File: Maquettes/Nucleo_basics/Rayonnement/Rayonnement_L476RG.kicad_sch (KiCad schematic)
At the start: 26 parts, among them J10 Morpho_Gauche, J11 Morpho_Droite, J19 GND_reg, J2 LED_POWER, J20 3.3V_reg, J23 D_IN_OUT, J7 Servo, J8 BAT_IN, Q1 IRLZ44N, SW1 SW_1, SW2 SW_2, U1 CNY17-3, U2 LM7805_TO220

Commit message: Update Rayonnement Schematics
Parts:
- removed Q1: IRLZ44N, Package_TO_SOT_THT:TO-220-3_Vertical, symbol Transistor_FET:IRLZ44N
- removed R4: 1k, symbol Device:R
- removed R6: 220, symbol Device:R
- removed U1: CNY17-3, symbol Isolator:CNY17-3
- added J1: LED_IN, TerminalBlock_Phoenix:TerminalBlock_Phoenix_MKDS-3-2-5.08_1x02_P5.08mm_Horizontal, symbol Connector_Generic:Conn_01x02
- added U1, U4: ~, Package_DIP:DIP-8_W7.62mm_LongPads, symbol LEnsE_devices:MCP4132
- added U3: BCR430UW6, Package_TO_SOT_SMD:SC-74-6_1.55x2.9mm_P0.95mm, symbol Driver_LED:BCR430UW6
- J2: value LED_POWER -> LED_OUT
- J8: value BAT_IN -> POWER_IN
- R3: value 680 -> 1k; footprint (none) -> Resistor_THT:R_Axial_DIN0207_L6.3mm_D2.5mm_P10.16mm_Horizontal
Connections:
- net GND1 is gone; now on net GND: R3.2
- net 3.3V_NUC: now also U4.6 (POB)
- net 5V_NUC: now also U1.8 (VDD), U4.8 (VDD)
- net GND: now also J1.1 (Pin_1), U1.4 (VSS), U1.5 (POW), U3.2 (GND), U4.4 (VSS)
- net VIN: no longer J2.1 (Pin_1)
- net POT_NUM_OUT: now reaches J10.40 (Pin_40)
- net POT_NUM_OUT: now also R3.1, U4.5 (POW)
- net SCK: now reaches J11.13 (Pin_13)
- net SCK: now also U1.2 (SCK), U4.2 (SCK)
- net MISO: now reaches J11.15 (Pin_15)
- net MISO: now also U1.7 (SDO/MISO), U4.7 (SDO/MISO)
- net MOSI: now reaches J11.17 (Pin_17)
- net MOSI: now also U1.3 (SDI/MOSI), U4.3 (SDI/MOSI)
- net CS_1: now reaches J11.19 (Pin_19)
- net CS_1: now also U1.1 (CS)
- net CS_2: now reaches J11.23 (Pin_23)
- net CS_2: now also U4.1 (CS)
- net at J2.2 (Pin_2): now also U3.6 (OUT)
- new net: U1.6 (POB), U3.3 (REXT)
- new net LED_POW_IN: J1.2 (Pin_2), J2.1 (Pin_1), U3.4 (VS)

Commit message: Update Rayonnement
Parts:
- added J6: PhotoDiode, Connector_PinHeader_2.54mm:PinHeader_1x02_P2.54mm_Vertical, symbol Connector_Generic:Conn_01x02
- added J9: Thermistance, Connector_PinHeader_2.54mm:PinHeader_1x02_P2.54mm_Vertical, symbol Connector_Generic:Conn_01x02
- added R4: 100k, Resistor_THT:R_Axial_DIN0207_L6.3mm_D2.5mm_P10.16mm_Horizontal, symbol Device:R
- added R5: 10k, Resistor_THT:R_Axial_DIN0207_L6.3mm_D2.5mm_P10.16mm_Horizontal, symbol Device:R
- added RV2: 100k, Potentiometer_THT:Potentiometer_Bourns_3386P_Vertical, symbol Device:R_Potentiometer
- J2: renamed from J7; footprint Connector_PinSocket_2.54mm:PinSocket_1x03_P2.54mm_Horizontal -> Connector_PinSocket_2.54mm:PinSocket_1x03_P2.54mm_Vertical
- renumbered J19 to J10, J20 to J11, J8 to J3, J10 to J4, J2 to J5, J11 to J7, J23 to J8, R5 to R3, R8 to R6, R3 to R7, U3 to U2, U2 to U3
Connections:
- net SCL is gone; now on net Servo: J7.5 (Pin_5)
- net SDA is gone; now on net CS_2: J7.7 (Pin_7)
- net 3.3V_NUC: now also J6.1 (Pin_1), R5.2
- net CS_1: now also J7.31 (Pin_31); no longer J7.19 (Pin_19)
- net CS_2: no longer J7.23 (Pin_23)
- net GND: now also J9.2 (Pin_2), RV2.3
- net POT_NUM_OUT: now also J4.36 (Pin_36); no longer J4.40 (Pin_40)
- net POT_OUT: now also J4.30 (Pin_30); no longer J4.39 (Pin_39)
- net SW1_OUT: now also J7.6 (Pin_6); no longer J7.16 (Pin_16)
- net SW2_OUT: now also J7.4 (Pin_4); no longer J7.14 (Pin_14)
- net Servo: no longer J4.23 (Pin_23)
- new net: R4.1, RV2.1, RV2.2
- new net PHD_OUT: J4.39 (Pin_39), J6.2 (Pin_2), R4.2
- new net RT_OUT: J4.40 (Pin_40), J9.1 (Pin_1), R5.1

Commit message: Update Robot and Lighting Diagram boards
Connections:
- net 5V: now also J2.2 (Pin_2); no longer J2.1 (Pin_1)
- net GND: now also J2.1 (Pin_1); no longer J2.2 (Pin_2)
- net POT_OUT: now also J7.36 (Pin_36); no longer J4.30 (Pin_30)
- net Servo: now also J4.23 (Pin_23); no longer J7.5 (Pin_5)
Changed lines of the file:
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@@
 	(wire
 		(pts
+			(xy 166.37 96.52) (xy 168.91 96.52)
+		)
+		(stroke
+			(width 0)
+			(type default)
+		)
+	)
+	(wire
+		(pts
 			(xy 36.83 135.89) (xy 36.83 138.43)
 		)
@@
 	(global_label "Servo"
 		(shape input)
-		(at 151.13 58.42 180)
+		(at 96.52 81.28 180)
 		(effects
 			(font
@@
 		)
 		(property "Intersheetrefs" "${INTERSHEET_REFS}"
-			(at 151.13 58.42 0)
+			(at 96.52 81.28 0)
 			(effects
 				(font
@@
 	(global_label "5V"
 		(shape input)
-		(at 55.88 30.48 180)
+		(at 55.88 33.02 180)
 		(effects
 			(font
@@
 		)
 		(property "Intersheetrefs" "${INTERSHEET_REFS}"
-			(at 55.88 30.48 0)
+			(at 55.88 33.02 0)
 			(effects
 				(font
@@
 	(global_label "POT_OUT"
 		(shape input)
-		(at 114.3 88.9 0)
+		(at 168.91 96.52 0)
 		(fields_autoplaced yes)
 		(effects
@@
 		)
 		(property "Intersheetrefs" "${INTERSHEET_REFS}"
-			(at 124.7953 88.9 0)
+			(at 179.4053 96.52 0)
 			(effects
 				(font
@@
 	(symbol
 		(lib_id "power:GND")
-		(at 55.88 33.02 270)
+		(at 55.88 30.48 270)
 		(unit 1)
 		(exclude_from_sim no)
@@
 		(dnp no)
 		(property "Reference" "#PWR06"
-			(at 49.53 33.02 0)
+			(at 49.53 30.48 0)
 			(effects
 				(font
@@
 		)
 		(property "Value" "GND"
-			(at 52.6288 33.147 90)
+			(at 52.6288 30.607 90)
 			(effects
 				(font
@@
 		)
 		(property "Footprint" ""
-			(at 55.88 33.02 0)
+			(at 55.88 30.48 0)
 			(effects
 				(font
@@
 		)
 		(property "Datasheet" ""
-			(at 55.88 33.02 0)
+			(at 55.88 30.48 0)
 			(effects
 				(font
@@
 		)
 		(property "Description" ""
-			(at 55.88 33.02 0)
+			(at 55.88 30.48 0)
 			(effects
 				(font

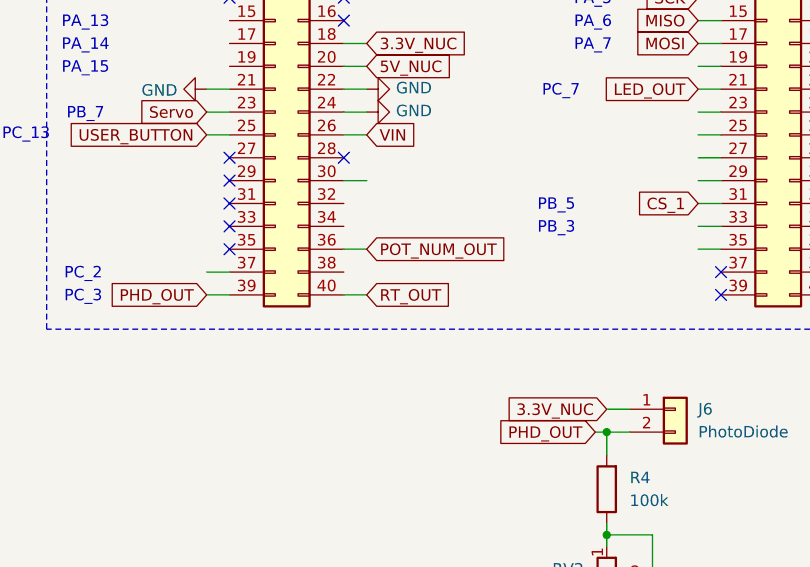
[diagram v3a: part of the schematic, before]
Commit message: Update Radiation DIagram Board
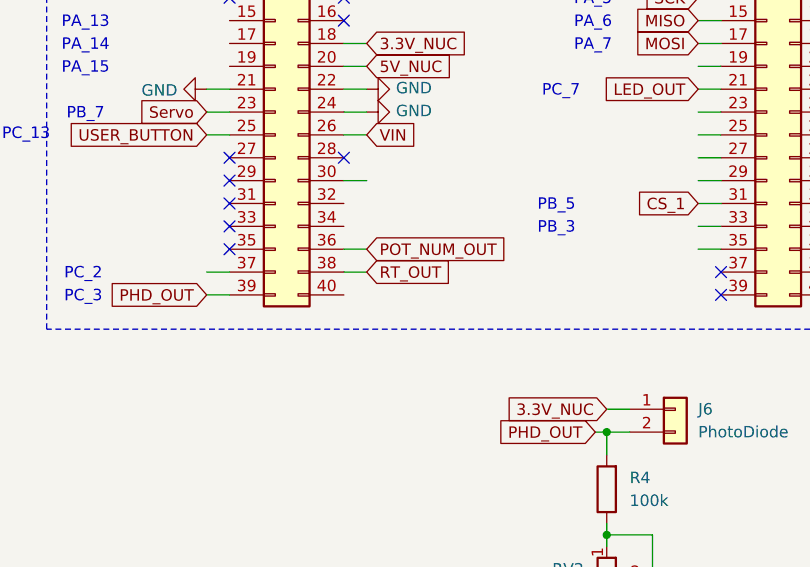
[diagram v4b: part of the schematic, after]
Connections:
- net RT_OUT: now also J4.38 (Pin_38); no longer J4.40 (Pin_40)
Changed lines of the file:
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@@
-	(wire
-		(pts
-			(xy 111.76 101.6) (xy 114.3 101.6)
-		)
-		(stroke
-			(width 0)
-			(type default)
-		)
-	)
 	(wire
 		(pts
@@
 		(pts
 			(xy 172.72 93.98) (xy 168.91 93.98)
+		)
+		(stroke
+			(width 0)
+			(type default)
+		)
+	)
+	(wire
+		(pts
+			(xy 111.76 99.06) (xy 114.3 99.06)
 		)
 		(stroke
@@
 	(global_label "RT_OUT"
 		(shape input)
-		(at 114.3 101.6 0)
+		(at 114.3 99.06 0)
 		(fields_autoplaced yes)
 		(effects
@@
 		)
 		(property "Intersheetrefs" "${INTERSHEET_REFS}"
-			(at 123.4648 101.6 0)
-			(effects
-				(font
+			(at 123.4648 99.06 0)
+			(effects
+				(font

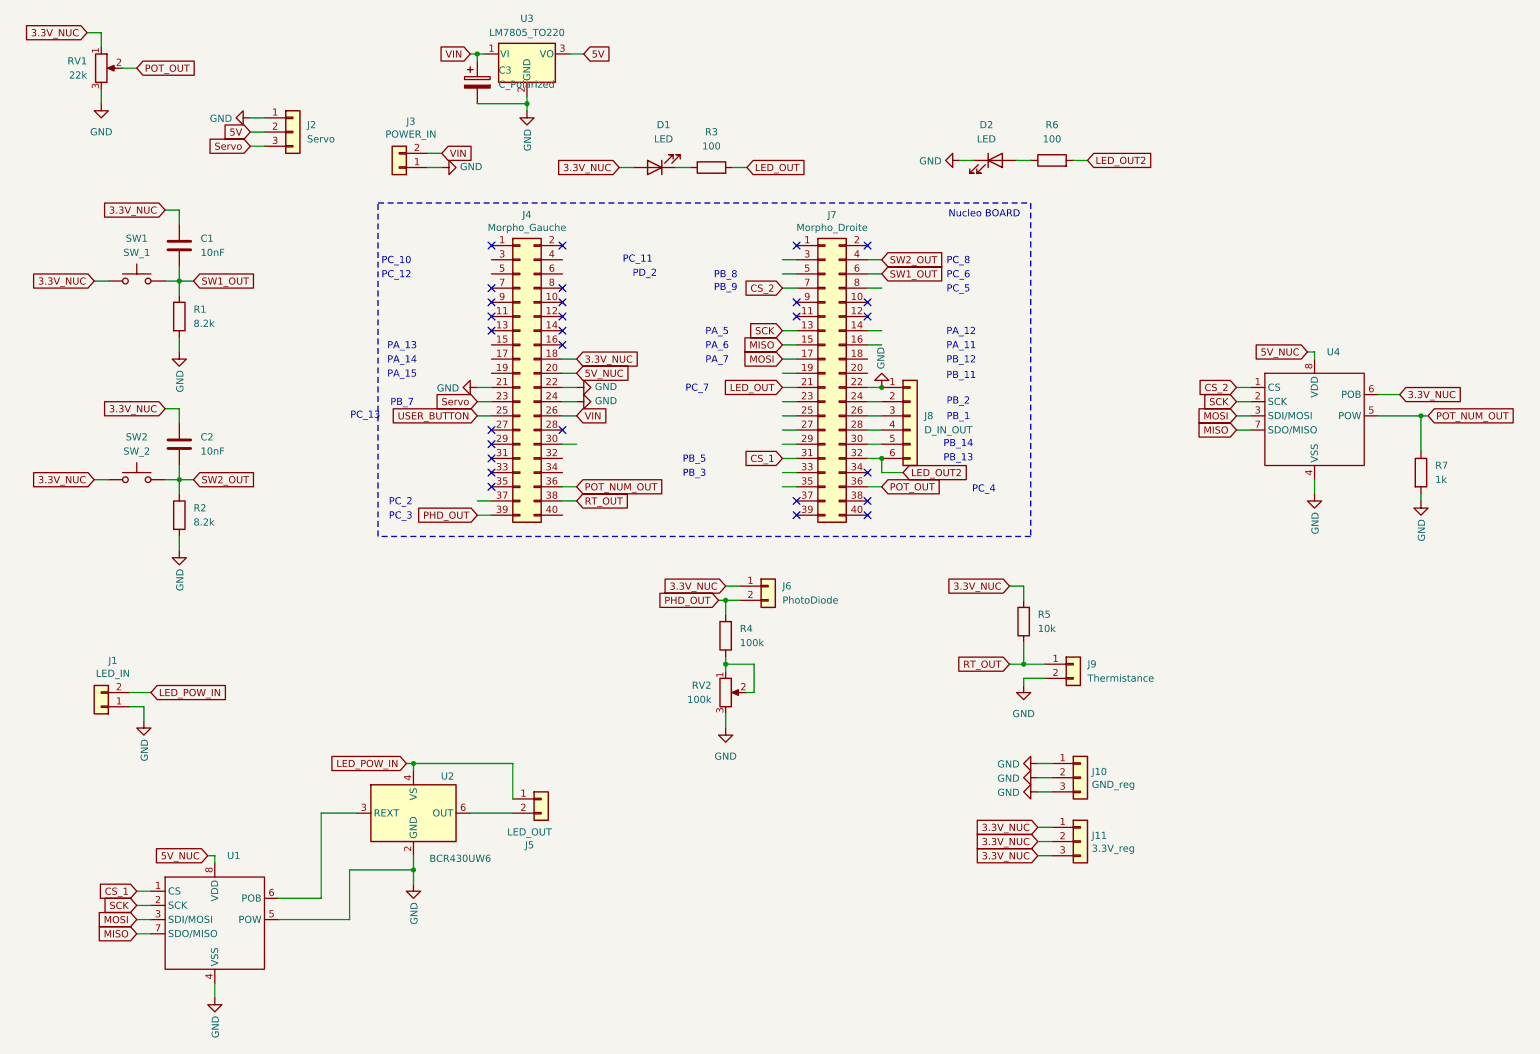
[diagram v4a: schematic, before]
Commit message: Update Rayonnement_L476RG.kicad_sch
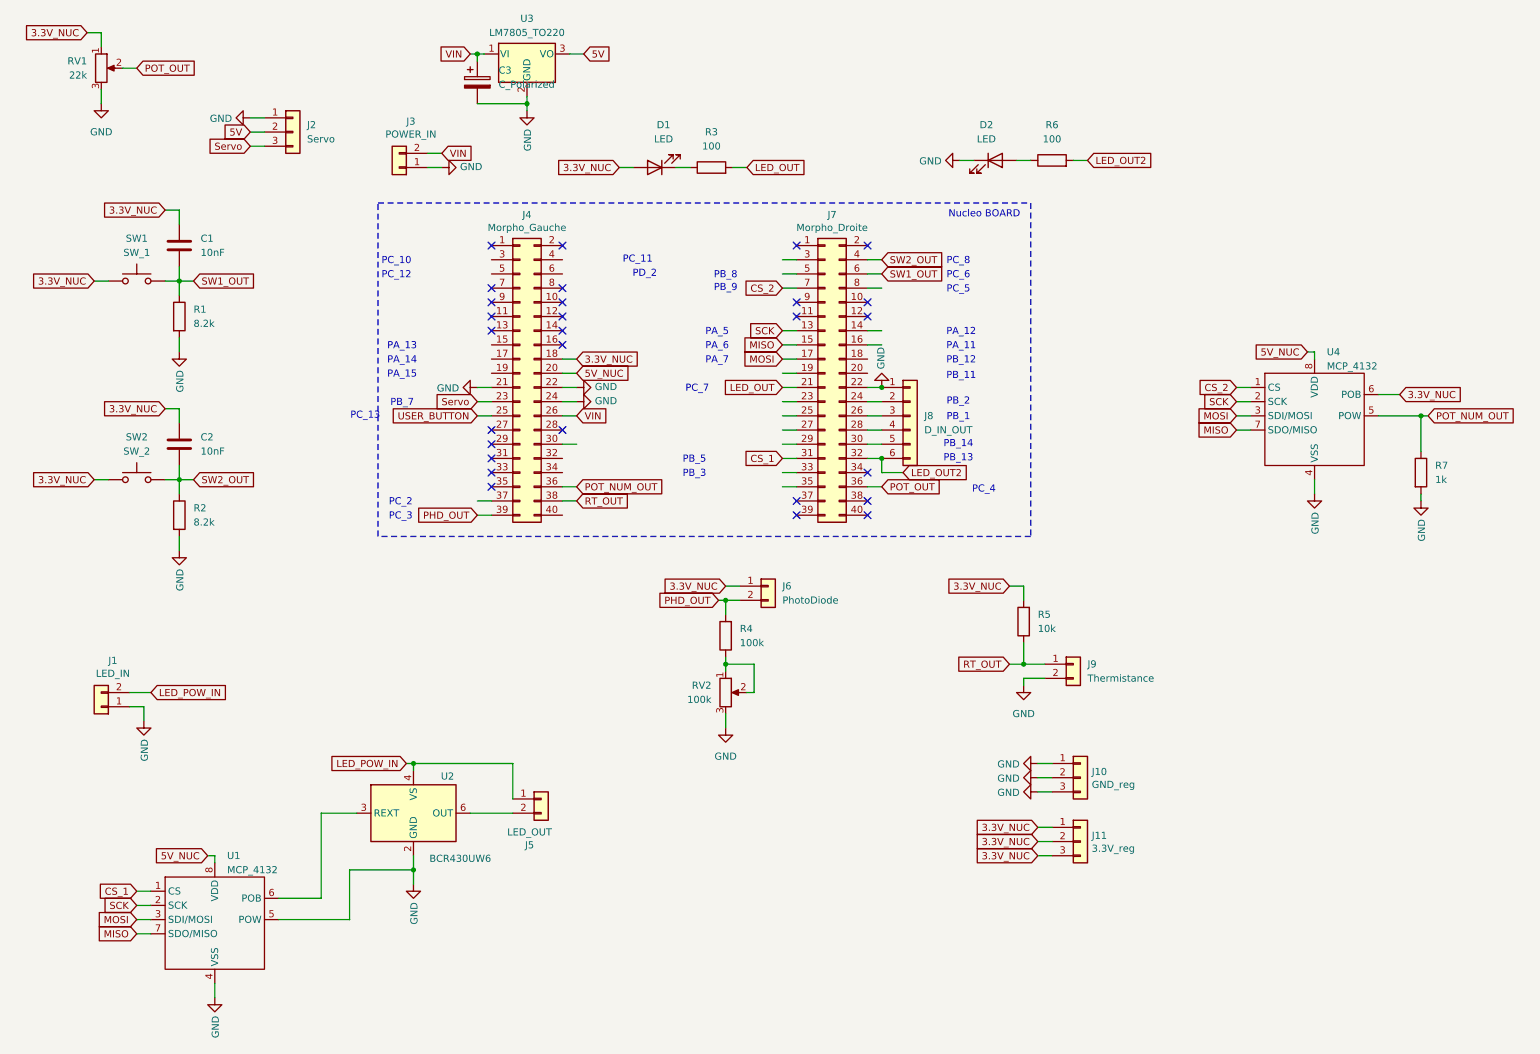
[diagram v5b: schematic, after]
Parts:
- U1, U4: value ~ -> MCP_4132
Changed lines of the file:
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@@
 			)
 		)
-		(property "Value" "~"
+		(property "Value" "MCP_4132"
 			(at 248.5741 74.93 0)
 			(effects
@@
 			)
 		)
-		(property "Value" "~"
+		(property "Value" "MCP_4132"
 			(at 51.7241 165.1 0)
 			(effects

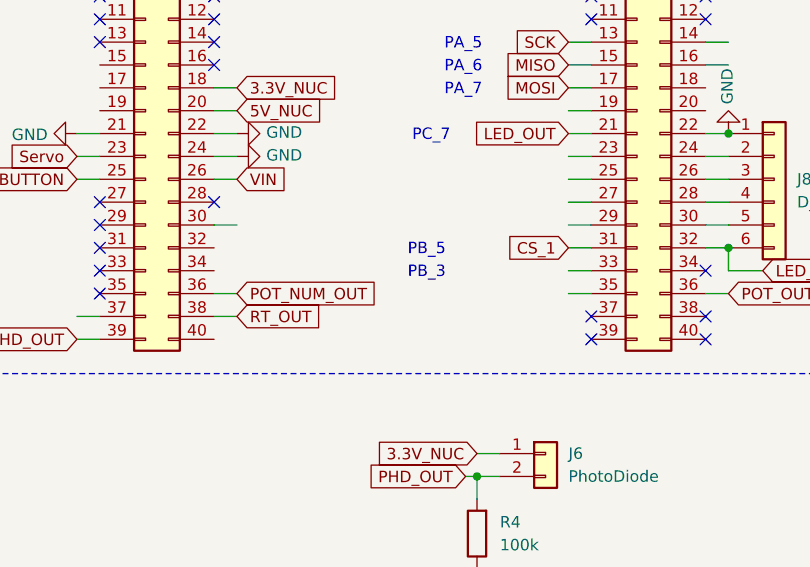
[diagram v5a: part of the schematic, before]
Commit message: Update Radiation board schematic
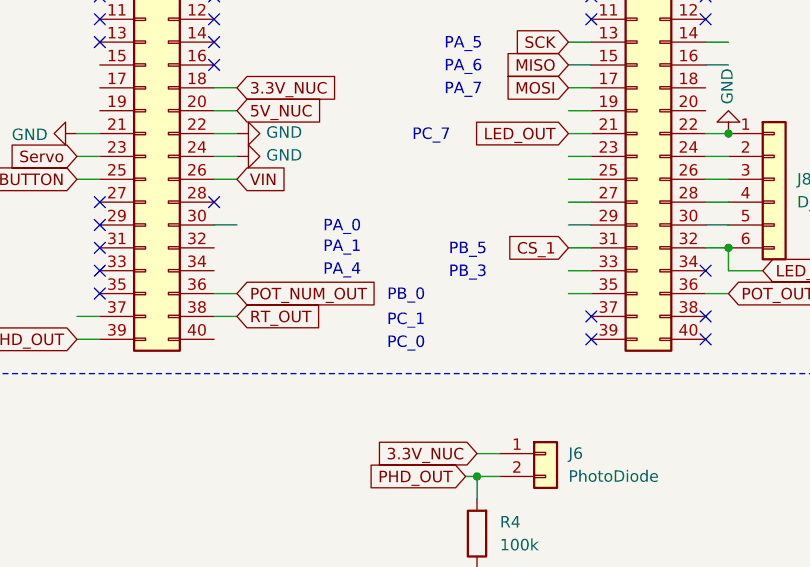
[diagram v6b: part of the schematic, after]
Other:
- note added: "PA_0"
- note added: "PA_1"
- note added: "PA_4"
- note added: "PB_0"
- note added: "PC_0"
- note added: "PC_1"
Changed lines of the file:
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@@
+		)
+	)
+	(text "PB_0"
+		(exclude_from_sim no)
+		(at 133.096 96.774 0)
+		(effects
+			(font
+				(size 1.27 1.27)
+			)
 		)
 	)
@@
 	(text "PB_3\n\n"
 		(exclude_from_sim no)
-		(at 135.382 95.25 0)
+		(at 139.954 95.25 0)
 		(effects
 			(font
@@
 		)
 	)
+	(text "PC_1"
+		(exclude_from_sim no)
+		(at 133.096 99.568 0)
+		(effects
+			(font
+				(size 1.27 1.27)
+			)
+		)
+	)
 	(text "PC_12"
 		(exclude_from_sim no)
@@
 		)
 	)
+	(text "PA_1"
+		(exclude_from_sim no)
+		(at 125.984 91.44 0)
+		(effects
+			(font
+				(size 1.27 1.27)
+			)
+		)
+	)
 	(text "Nucleo BOARD"
 		(exclude_from_sim no)
@@
 		)
 	)
+	(text "PC_0"
+		(exclude_from_sim no)
+		(at 133.096 102.108 0)
+		(effects
+			(font
+				(size 1.27 1.27)
+			)
+		)
+	)
 	(text "PB_12"
 		(exclude_from_sim no)
@@
 		)
 	)
+	(text "PA_0"
+		(exclude_from_sim no)
+		(at 125.984 89.154 0)
+		(effects
+			(font
+				(size 1.27 1.27)
+			)
+		)
+	)
+	(text "PA_4"
+		(exclude_from_sim no)
+		(at 125.984 93.98 0)
+		(effects
+			(font
+				(size 1.27 1.27)
+			)
+		)
+	)
 	(text "PC_6"
 		(exclude_from_sim no)
@@
 	(text "PB_5\n\n"
 		(exclude_from_sim no)
-		(at 135.382 92.71 0)
-		(effects
-			(font
+		(at 139.954 92.71 0)
+		(effects
+			(font

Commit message: Update Radiation Board schematic
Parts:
- R7: value 1k -> 10k
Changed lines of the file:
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@@
 			)
 		)
-		(property "Value" "1k"
+		(property "Value" "10k"
 			(at 267.97 95.2499 0)
 			(effects
